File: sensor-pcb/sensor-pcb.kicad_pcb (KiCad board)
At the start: 2 copper layers, 22.8 x 27.6 mm, 18 parts, among them J1 Conn_01x03, J2 Conn_01x02, J3 Conn_01x01_Socket, J4 Conn_01x01_Socket, Q2 BSS84, U1 TLV2371DBV

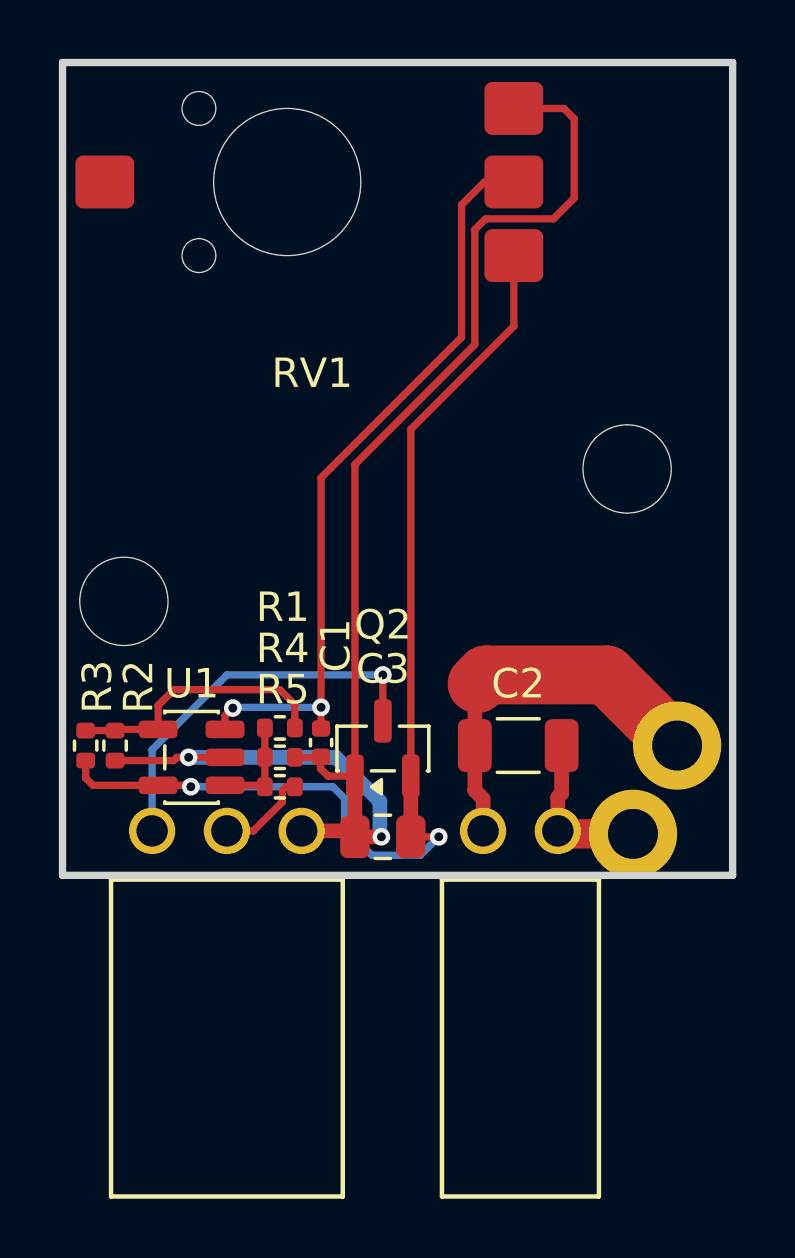
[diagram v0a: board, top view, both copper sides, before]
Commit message: Fix flipped power pins
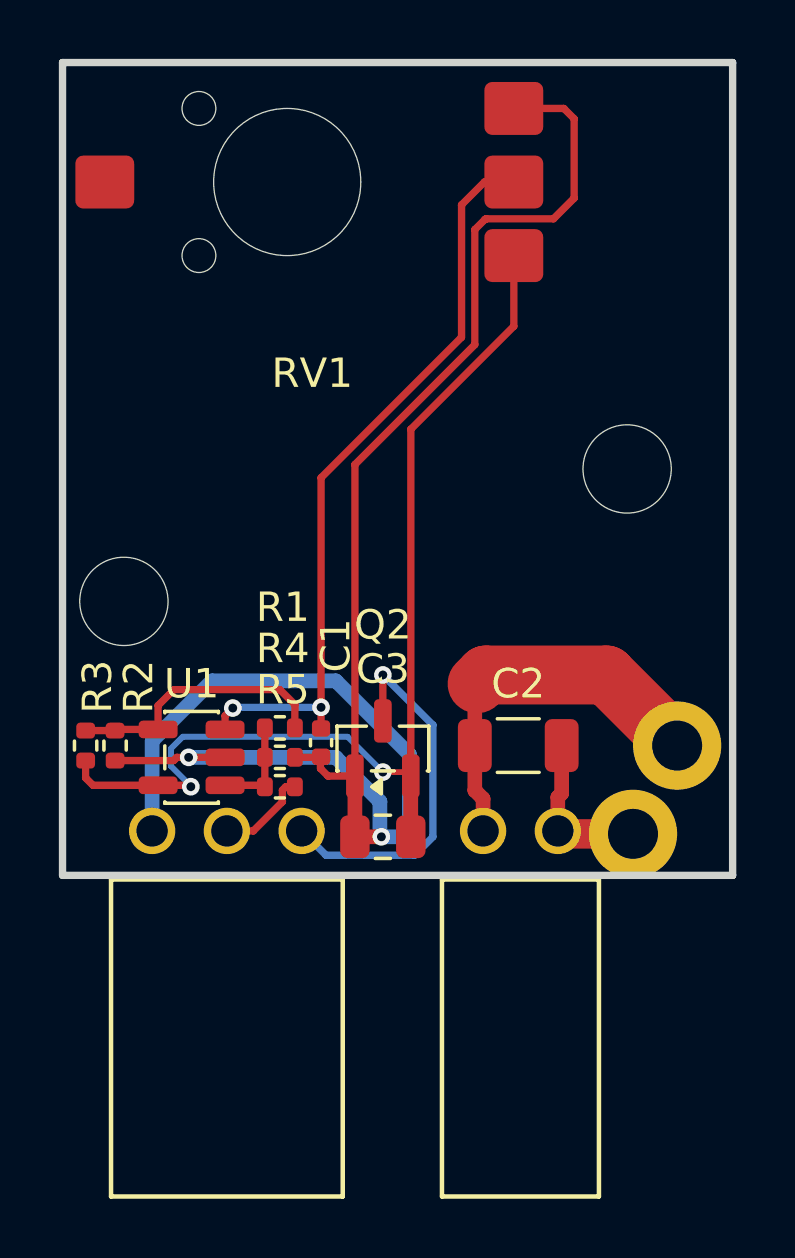
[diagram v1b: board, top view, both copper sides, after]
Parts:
- RV1: value 10k -> RDC503052A
- U1: value TLV2371DBV -> TLV9151IDBVR
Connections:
- J1 pad 1: GND -> /VIN
- J1 pad 3: /VIN -> GND
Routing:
- net GND: track 48.6 -> 64.3 mm
- net +5V: track 36.7 -> 35.9 mm
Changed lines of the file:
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@@
 			)
 		)
-		(property "Value" "10k"
+		(property "Value" "RDC503052A"
 			(at 0 10 90)
 			(unlocked yes)
@@
 			(layers "*.Cu" "*.Mask")
 			(remove_unused_layers no)
-			(net 1 "GND")
+			(net 5 "/VIN")
 			(pinfunction "Pin_1")
 			(pintype "passive")
@@
 			(layers "*.Cu" "*.Mask")
 			(remove_unused_layers no)
-			(net 5 "/VIN")
+			(net 1 "GND")
 			(pinfunction "Pin_3")
 			(pintype "passive")
@@
 			)
 		)
-		(property "Value" "TLV2371DBV"
+		(property "Value" "TLV9151IDBVR"
 			(at 0 2.4 0)
 			(layer "F.Fab")
@@
 			)
 		)
-		(property "MPN" "TLV2371DBV"
+		(property "MPN" "TLV9151IDBVR"
 			(at 0 0 180)
 			(unlocked yes)
@@
 	)
 	(segment
-		(start 170.625 105.11)
-		(end 172.235 105.11)
-		(width 0.5)
-		(layer "F.Cu")
-		(net 1)
-	)
-	(segment
 		(start 166.385 102.61)
 		(end 168.0225 102.61)
@@
 	)
 	(segment
+		(start 165.545 102.05)
+		(end 165.545 105.11)
+		(width 0.5)
+		(layer "B.Cu")
+		(net 1)
+	)
+	(segment
 		(start 173.335 105.31)
 		(end 173.285 105.26)
@@
 	)
 	(segment
+		(start 167.585 100.01)
+		(end 165.545 102.05)
+		(width 0.5)
+		(layer "B.Cu")
+		(net 1)
+	)
+	(segment
+		(start 173.335 105.31)
+		(end 173.985 105.31)
+		(width 0.5)
+		(layer "B.Cu")
+		(net 1)
+	)
+	(segment
+		(start 171.785 100.01)
+		(end 167.585 100.01)
+		(width 0.5)
+		(layer "B.Cu")
+		(net 1)
+	)
+	(segment
 		(start 171.785 102.61)
 		(end 166.785 102.61)
@@
 	)
 	(segment
+		(start 173.985 105.31)
+		(end 174.285 105.01)
+		(width 0.5)
+		(layer "B.Cu")
+		(net 1)
+	)
+	(segment
+		(start 174.285 105.01)
+		(end 174.285 102.51)
+		(width 0.5)
+		(layer "B.Cu")
+		(net 1)
+	)
+	(segment
+		(start 174.285 102.51)
+		(end 171.785 100.01)
+		(width 0.5)
+		(layer "B.Cu")
+		(net 1)
+	)
+	(segment
 		(start 173.285 105.26)
 		(end 173.285 104.11)
@@
 	)
 	(segment
-		(start 175.285 105.31)
-		(end 174.335 105.31)
-		(width 0.25)
+		(start 174.1975 103.11)
+		(end 174.335 103.2475)
+		(width 0.2)
 		(layer "F.Cu")
 		(net 4)
@@
 	)
 	(segment
+		(start 173.385 103.11)
+		(end 174.1975 103.11)
+		(width 0.2)
+		(layer "F.Cu")
+		(net 4)
+	)
+	(segment
 		(start 163.285 103.31)
 		(end 163.285 102.72)
@@
 	)
 	(via
-		(at 175.285 105.31)
+		(at 173.385 103.11)
 		(size 0.6)
 		(drill 0.3)
@@
 	)
 	(segment
-		(start 172.085 104.01)
-		(end 172.085 105.01)
-		(width 0.25)
+		(start 172.185 101.91)
+		(end 166.585 101.91)
+		(width 0.2)
 		(layer "B.Cu")
 		(net 4)
 	)
 	(segment
-		(start 173.011 105.936)
-		(end 174.659 105.936)
-		(width 0.25)
+		(start 173.385 103.11)
+		(end 172.185 101.91)
+		(width 0.2)
 		(layer "B.Cu")
 		(net 4)
 	)
 	(segment
-		(start 166.86 103.607339)
-		(end 171.682339 103.607339)
-		(width 0.25)
+		(start 166.585 101.91)
+		(end 166.185 102.31)
+		(width 0.2)
 		(layer "B.Cu")
 		(net 4)
 	)
 	(segment
-		(start 174.659 105.936)
-		(end 175.285 105.31)
-		(width 0.25)
+		(start 166.185 102.31)
+		(end 166.185 102.91)
+		(width 0.2)
 		(layer "B.Cu")
 		(net 4)
 	)
 	(segment
-		(start 172.085 105.01)
-		(end 173.011 105.936)
-		(width 0.25)
+		(start 166.185 102.91)
+		(end 166.86 103.585)
+		(width 0.2)
 		(layer "B.Cu")
 		(net 4)
 	)
 	(segment
-		(start 171.682339 103.607339)
-		(end 172.085 104.01)
-		(width 0.25)
+		(start 166.86 103.585)
+		(end 166.86 103.607339)
+		(width 0.2)
 		(layer "B.Cu")
 		(net 4)
@@
 	)
 	(segment
-		(start 168.085 99.81)
-		(end 173.385 99.81)
+		(start 171.451 105.936)
+		(end 170.625 105.11)
 		(width 0.25)
 		(layer "B.Cu")
@@
 	)
 	(segment
-		(start 165.545 105.11)
-		(end 165.545 102.35)
+		(start 175.085 105.31)
+		(end 174.459 105.936)
 		(width 0.25)
 		(layer "B.Cu")
@@
 	)
 	(segment
-		(start 165.545 102.35)
-		(end 168.085 99.81)
+		(start 173.385 99.81)
+		(end 175.085 101.51)
 		(width 0.25)
 		(layer "B.Cu")
+		(net 5)
+	)
+	(segment
+		(start 175.085 101.51)
+		(end 175.085 105.31)
+		(width 0.25)
+		(layer "B.Cu")
+		(net 5)
+	)
+	(segment
+		(start 174.459 105.936)
+		(end 171.451 105.936)
+		(width 0.25)
+		(layer "B.Cu")

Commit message: Reverse direction
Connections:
- RV1 pad 1: +5V -> GND
- RV1 pad 3: GND -> +5V
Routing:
- net GND: track 64.3 -> 55.2 mm
- net +5V: track 35.9 -> 43.0 mm
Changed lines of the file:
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@@
 			(layers "F.Cu" "F.Mask" "F.Paste")
 			(roundrect_rratio 0.15)
-			(net 4 "+5V")
+			(net 1 "GND")
 			(pinfunction "1")
 			(pintype "passive")
@@
 			(layers "F.Cu" "F.Mask" "F.Paste")
 			(roundrect_rratio 0.15)
-			(net 1 "GND")
+			(net 4 "+5V")
 			(pinfunction "3")
 			(pintype "passive")
@@
 	)
 	(segment
+		(start 172.435 103.2475)
+		(end 172.435 92.66)
+		(width 0.25)
+		(layer "F.Cu")
+		(net 1)
+	)
+	(segment
 		(start 172.235 105.11)
 		(end 172.435 105.31)
@@
 	)
 	(segment
-		(start 179.535 80.56)
-		(end 179.885 80.91)
-		(width 0.25)
-		(layer "F.Cu")
-		(net 1)
-	)
-	(segment
 		(start 172.435 103.2475)
 		(end 172.435 105.31)
@@
 	)
 	(segment
-		(start 176.861 84.334)
-		(end 176.850648 84.334)
-		(width 0.25)
-		(layer "F.Cu")
-		(net 1)
-	)
-	(segment
-		(start 172.435 92.66)
-		(end 172.435 103.2475)
-		(width 0.25)
-		(layer "F.Cu")
-		(net 1)
-	)
-	(segment
-		(start 179.885 80.91)
-		(end 179.885 83.61)
+		(start 177.835 87.26)
+		(end 177.835 85.56)
 		(width 0.25)
 		(layer "F.Cu")
@@
 	)
 	(segment
-		(start 176.509 88.586)
-		(end 172.435 92.66)
-		(width 0.25)
-		(layer "F.Cu")
-		(net 1)
-	)
-	(segment
 		(start 171.5225 103.2475)
 		(end 172.435 103.2475)
@@
 	)
 	(segment
-		(start 179.185 84.31)
-		(end 176.885 84.31)
-		(width 0.25)
-		(layer "F.Cu")
-		(net 1)
-	)
-	(segment
-		(start 177.835 80.56)
-		(end 179.535 80.56)
-		(width 0.25)
-		(layer "F.Cu")
-		(net 1)
-	)
-	(segment
 		(start 164.285 102.72)
 		(end 166.275 102.72)
@@
 	)
 	(segment
-		(start 179.885 83.61)
-		(end 179.185 84.31)
-		(width 0.25)
-		(layer "F.Cu")
-		(net 1)
-	)
-	(segment
-		(start 176.885 84.31)
-		(end 176.861 84.334)
+		(start 172.435 92.66)
+		(end 177.835 87.26)
 		(width 0.25)
 		(layer "F.Cu")
@@
 		(start 171.265 102.61)
 		(end 171.285 102.59)
-		(width 0.25)
-		(layer "F.Cu")
-		(net 1)
-	)
-	(segment
-		(start 176.850648 84.334)
-		(end 176.509 84.675648)
-		(width 0.25)
-		(layer "F.Cu")
-		(net 1)
-	)
-	(segment
-		(start 176.509 84.675648)
-		(end 176.509 88.586)
 		(width 0.25)
 		(layer "F.Cu")
@@
 	)
 	(segment
+		(start 179.485 86.31)
+		(end 179.485 81.01)
+		(width 0.25)
+		(layer "F.Cu")
+		(net 4)
+	)
+	(segment
 		(start 174.1975 103.11)
 		(end 174.335 103.2475)
@@
 	)
 	(segment
-		(start 177.835 87.96)
-		(end 177.835 85.56)
-		(width 0.25)
-		(layer "F.Cu")
-		(net 4)
-	)
-	(segment
 		(start 165.7475 103.56)
 		(end 166.812661 103.56)
@@
 	(segment
 		(start 174.335 91.46)
-		(end 177.835 87.96)
+		(end 179.485 86.31)
 		(width 0.25)
 		(layer "F.Cu")
@@
 	)
 	(segment
+		(start 179.485 81.01)
+		(end 179.035 80.56)
+		(width 0.25)
+		(layer "F.Cu")
+		(net 4)
+	)
+	(segment
 		(start 166.812661 103.56)
 		(end 166.86 103.607339)
 		(width 0.25)
 		(layer "F.Cu")
+		(net 4)
+	)
+	(segment
+		(start 179.035 80.56)
+		(end 177.835 80.56)
+		(width 0.25)
+		(layer "F.Cu")

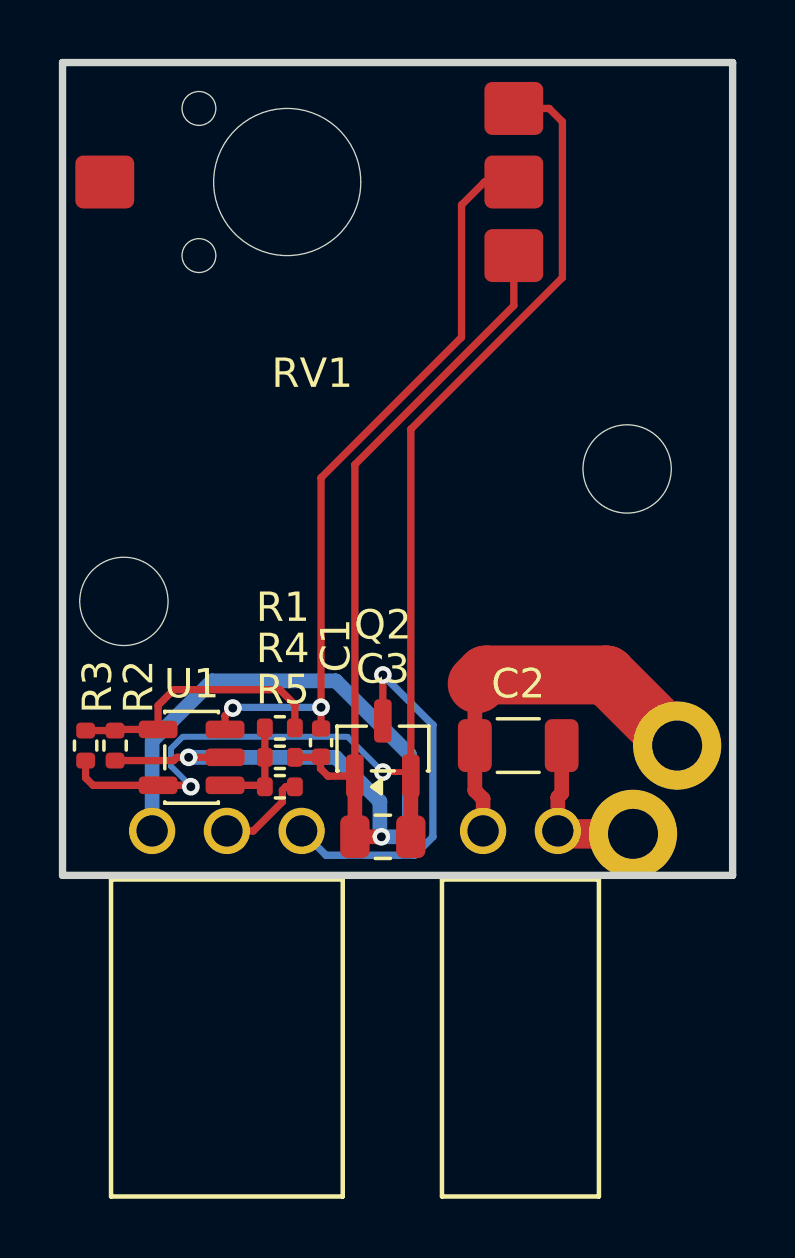
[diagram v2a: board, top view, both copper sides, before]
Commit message: Change design to allow arbitrary polarity
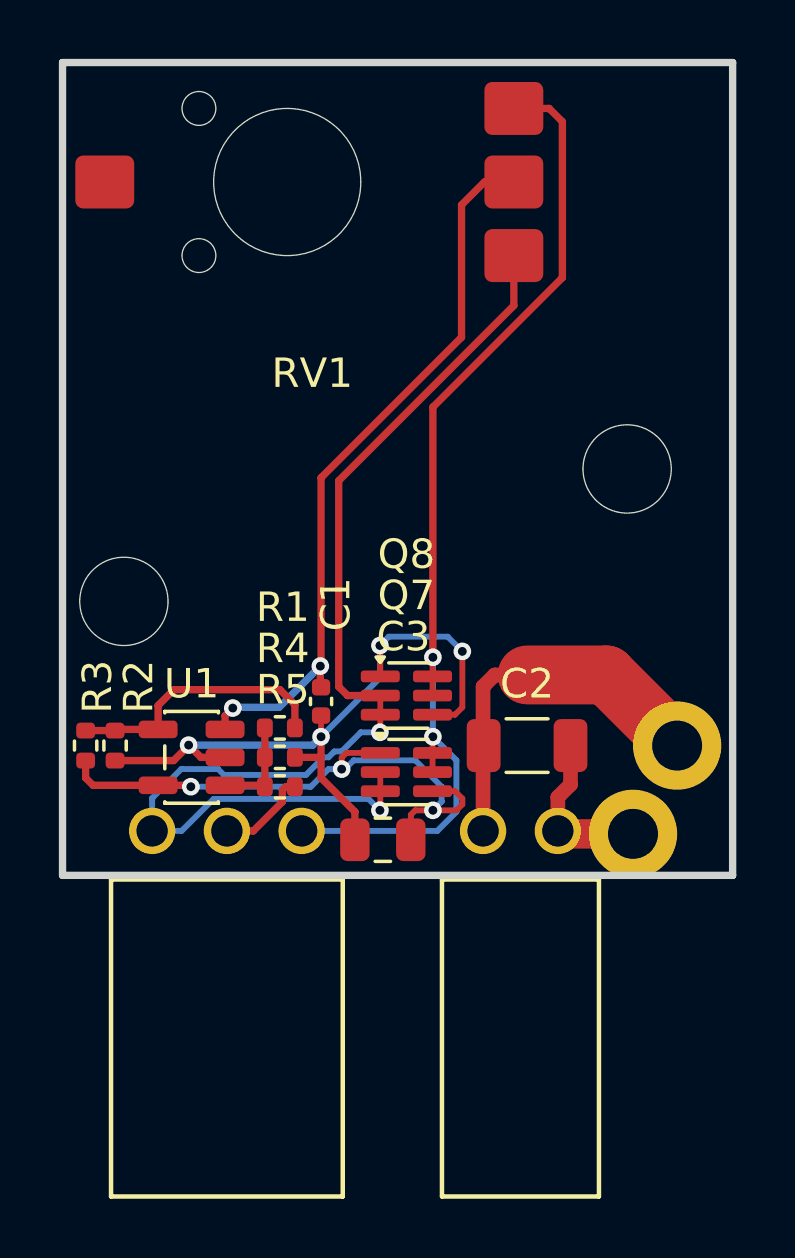
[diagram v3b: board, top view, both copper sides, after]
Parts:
- removed Q2: BSS84, Package_TO_SOT_SMD:SOT-23
- added Q7: BSS84DW-7-F, Package_TO_SOT_SMD:SOT-363_SC-70-6, F.Cu at (174.2, 103.1)
- added Q8: 2N7002DW, Package_TO_SOT_SMD:SOT-363_SC-70-6, F.Cu at (174.2, 100.5)
- moved C1 1.40 mm to (171.3, 100.7)
- moved C2 0.30 mm to (178.3, 102.2)
- moved C3 0.10 mm to (173.4, 105.4)
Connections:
- J1 pad 1: /VIN -> /VIN1
- J1 pad 3: GND -> /VIN2
- RV1 pad 1: GND -> /VIN2
- RV1 pad 3: +5V -> /VIN1
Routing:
- net /VIN2: track 0.00 -> 39.5 mm, vias 0 -> 2
- net /VIN1: track 0.00 -> 35.5 mm, vias 0 -> 2
- net GND: track 55.2 -> 25.8 mm, vias 2 -> 4
- net +5V: track 43.0 -> 20.3 mm, vias 2 -> 3
- net /VIN: track 12.8 -> 0.00 mm, vias 1 -> 0
- net /VPOS: track 25.7 -> 24.9 mm
